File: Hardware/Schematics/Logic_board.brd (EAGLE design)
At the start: 48.5 x 49 mm, 42 parts, among them IC1 ADUM1250, J1 1X2-3.5MM, J2 3-PIN SMD, J3 3-PIN SMD, J4 3-PIN SMD, U1 ESP-32S

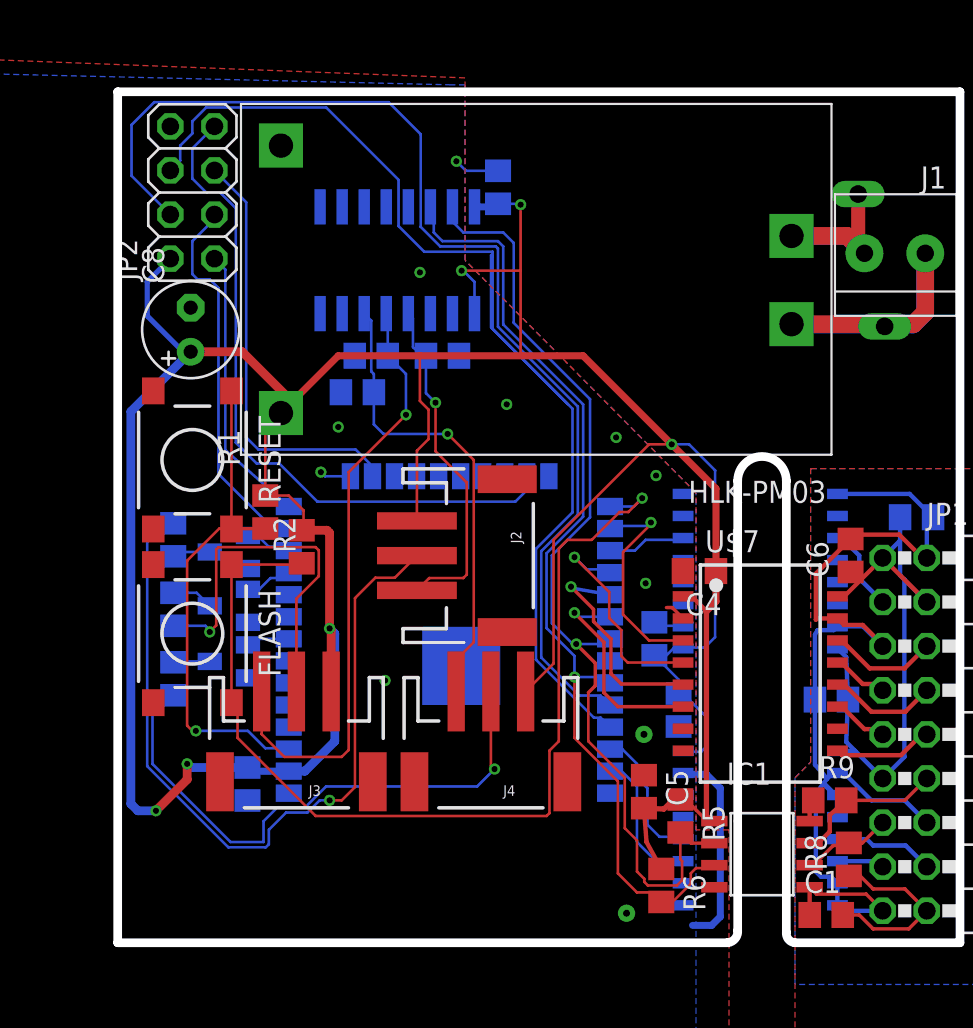
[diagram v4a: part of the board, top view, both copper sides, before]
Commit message: Work on changeing to FATFS. Not tested yet.
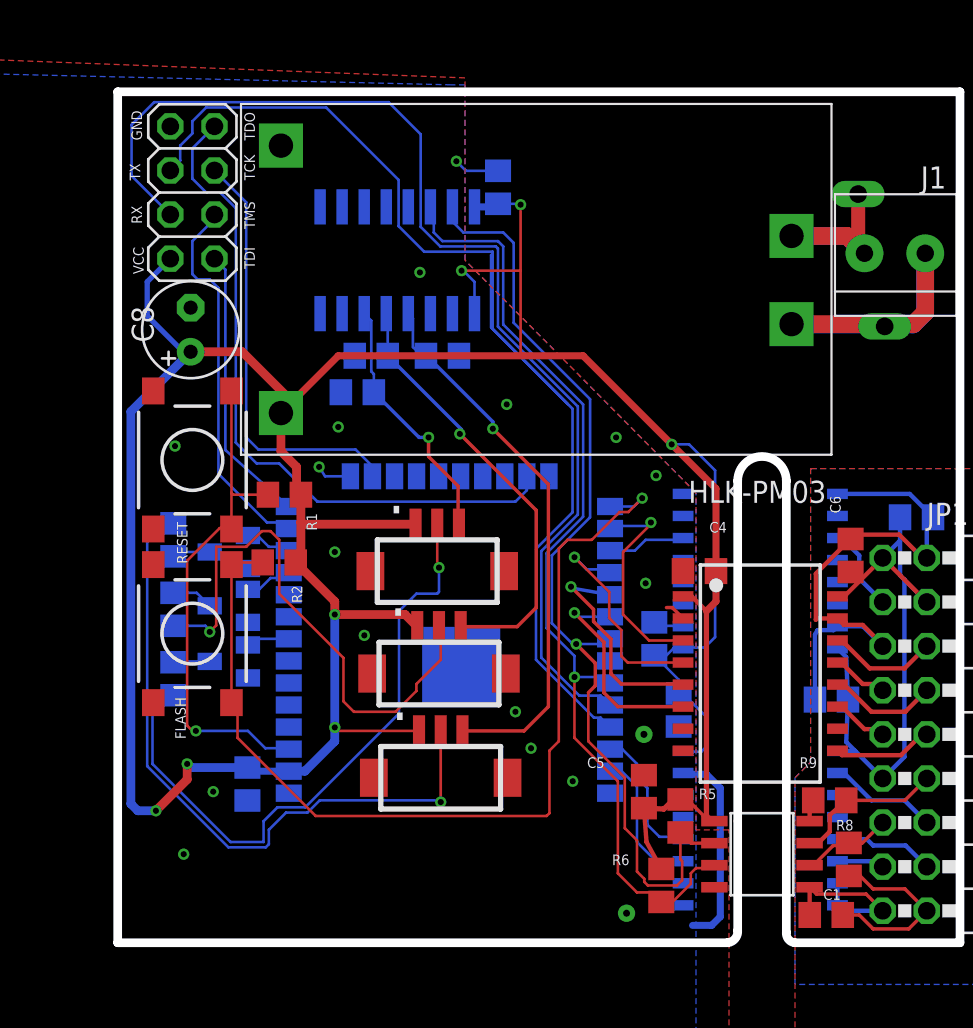
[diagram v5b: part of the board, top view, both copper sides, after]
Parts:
- removed J2, J3, J4: 3-PIN SMD, SparkFun-Connectors:JST-3-SMD
- added BUTTON1, BUTTON2, BUTTON3: DF13-3P-1.25V, con-hirose-df13:DF13C-3P-1.25V
- R11: value S14K11 -> 380V
- SUPPLY: value HLK-PM03 -> 5V
- moved R2 1.58 mm to (9.30, 21.9), turned to 180 degrees
- moved R1 1.49 mm to (9.60, 25.8), turned to 0 degrees
- renumbered U$8 to SUPPLY
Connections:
- net BUTTON1: now also BUTTON1.P$3; no longer J2.3
- net BUTTON2: now also BUTTON2.P$3; no longer J3.3
- net BUTTON3: now also BUTTON3.P$3; no longer J4.3
- net N$11: now also BUTTON3.P$2; no longer J4.2
- net N$7: now also BUTTON2.P$2; no longer J3.2
- net N$9: now also BUTTON1.P$2; no longer J2.2
- net VCC: now also BUTTON1.P$1, BUTTON2.P$1, BUTTON3.P$1; no longer J2.1, J3.1, J4.1
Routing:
- net VCC: track 213.1 -> 195.7 mm, vias 6 -> 7
- net GND1: track 70.0 -> 56.3 mm
- net BUTTON3: track 27.0 -> 14.9 mm
- net BUTTON1: track 19.8 -> 31.7 mm
- net BUTTON2: track 35.2 -> 25.4 mm
- net N$7: track 21.9 -> 31.7 mm
- net N$9: track 46.4 -> 39.6 mm
- net N$11: track 33.6 -> 37.4 mm
- net FLASH: track 57.6 -> 55.4 mm
- net N$66: track 31.1 -> 29.6 mm
- net GND: track 19.2 -> 19.5 mm, vias 11 -> 17
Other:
- board text added: "GND"
- board text added: "RX"
- board text added: "TCK"
- board text added: "TDI"
- board text added: "TDO"
- board text added: "TMS"
- board text added: "TX"
- board text added: "VCC"

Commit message: Migrated filesystem to FAT32.
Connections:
- net GND: now also U1.6, U1.7
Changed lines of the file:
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@@
 <via x="3.3" y="28.6" extent="1-16" drill="0.35"/>
 <via x="12.5" y="22.5" extent="1-16" drill="0.35"/>
+<contactref element="U1" pad="6"/>
+<contactref element="U1" pad="7"/>
 </signal>
 <signal name="VCC">

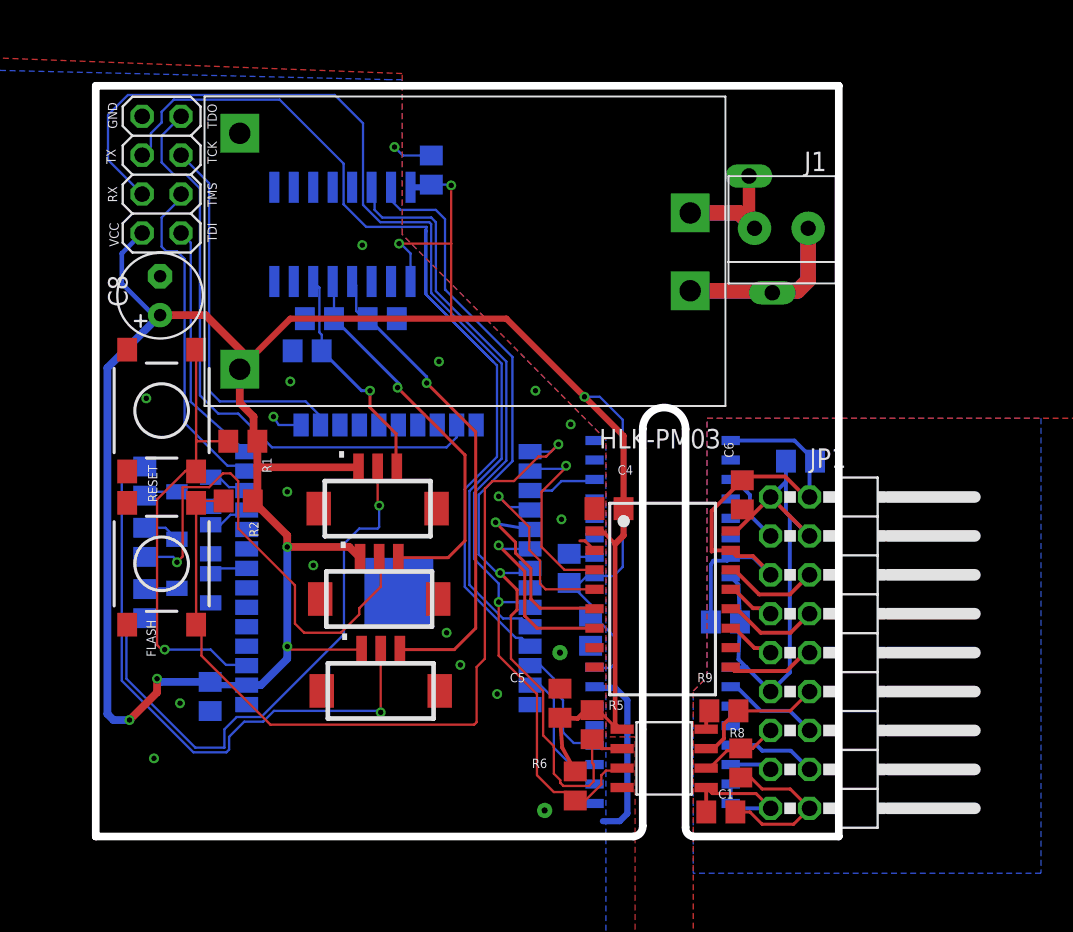
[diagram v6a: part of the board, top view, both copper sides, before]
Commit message: Updated board versions to final (v1) version, and added renders.
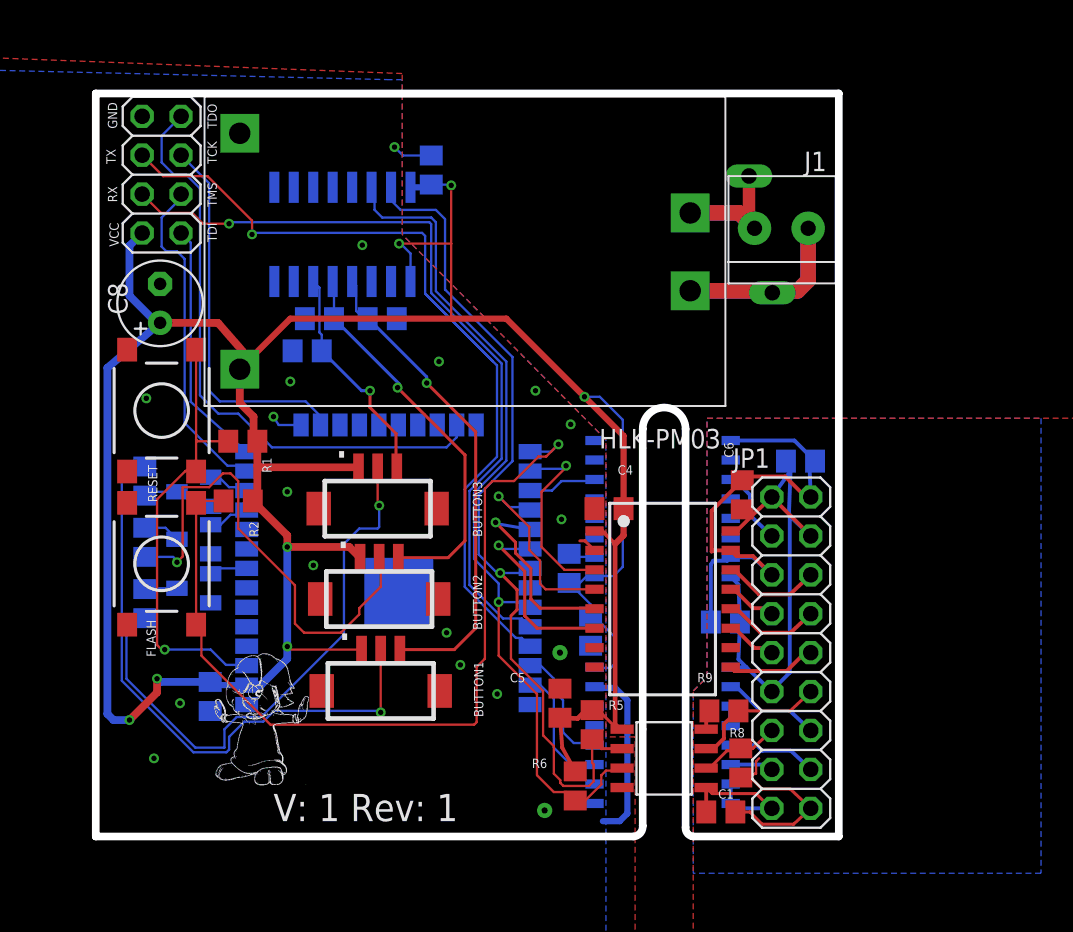
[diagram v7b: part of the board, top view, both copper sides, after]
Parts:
- JP1: device pinhead:2X09/90 -> pinhead:2X09
- moved JP1 5.00 mm to (45.4, 12.0)
- moved C8 0.50 mm to (4.20, 34.8)
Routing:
- net RX: track 65.8 -> 51.2 mm, vias 0 -> 1
- net TX: track 68.7 -> 59.0 mm, vias 0 -> 1
- net +5V: track 48.6 -> 51.2 mm
- net GND1: track 56.3 -> 56.8 mm
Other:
- board size 48.5 x 49 mm -> 48.5 x 48.5 mm
- board text added: "BUTTON1"
- board text added: "BUTTON2"
- board text added: "BUTTON3"
- board text added: "V: 1 Rev: 1"
